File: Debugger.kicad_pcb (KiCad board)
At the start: 2 copper layers, 22 parts, among them J1 Header internal clock, J2 I/O, Q1 BC546, SW1 Single step, U1 NE555P, U2 74LS00, U3 74LS74

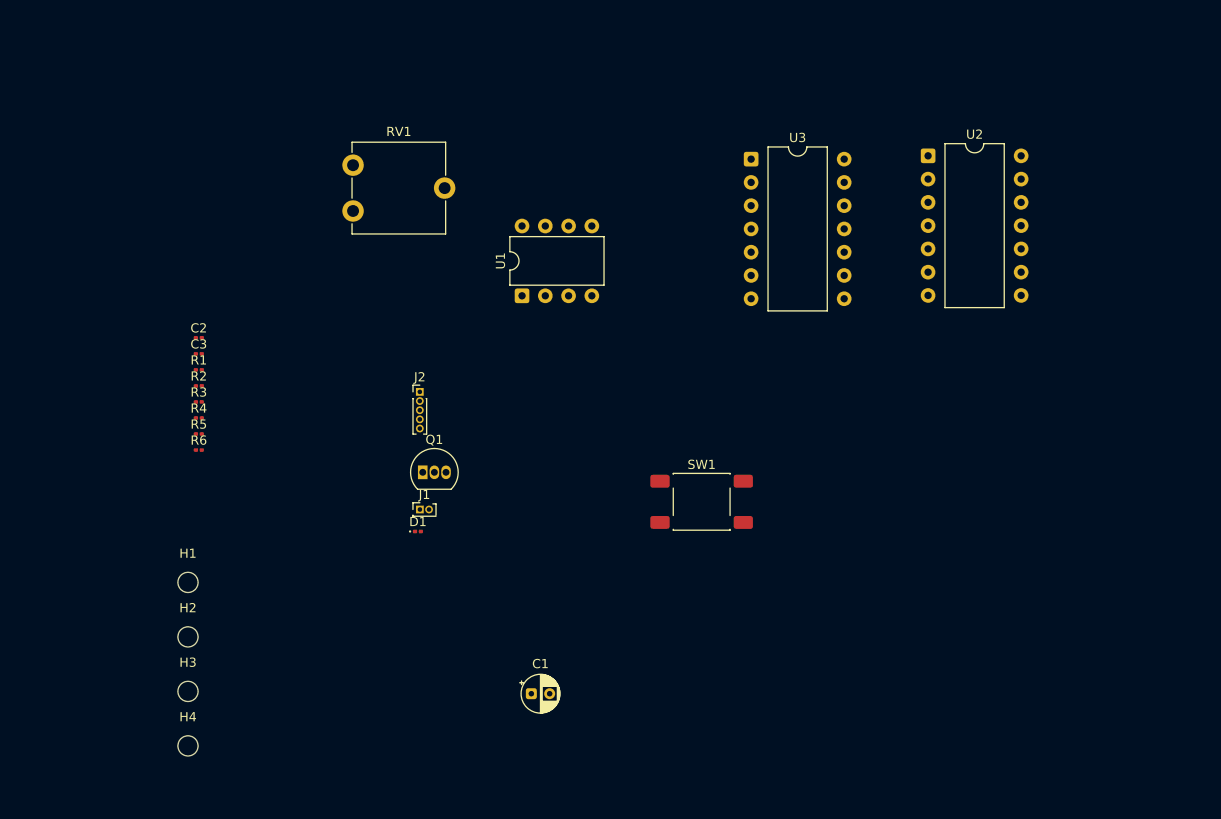
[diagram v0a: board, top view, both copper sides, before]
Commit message: Schematic: schmitt trigger, auxilary ports
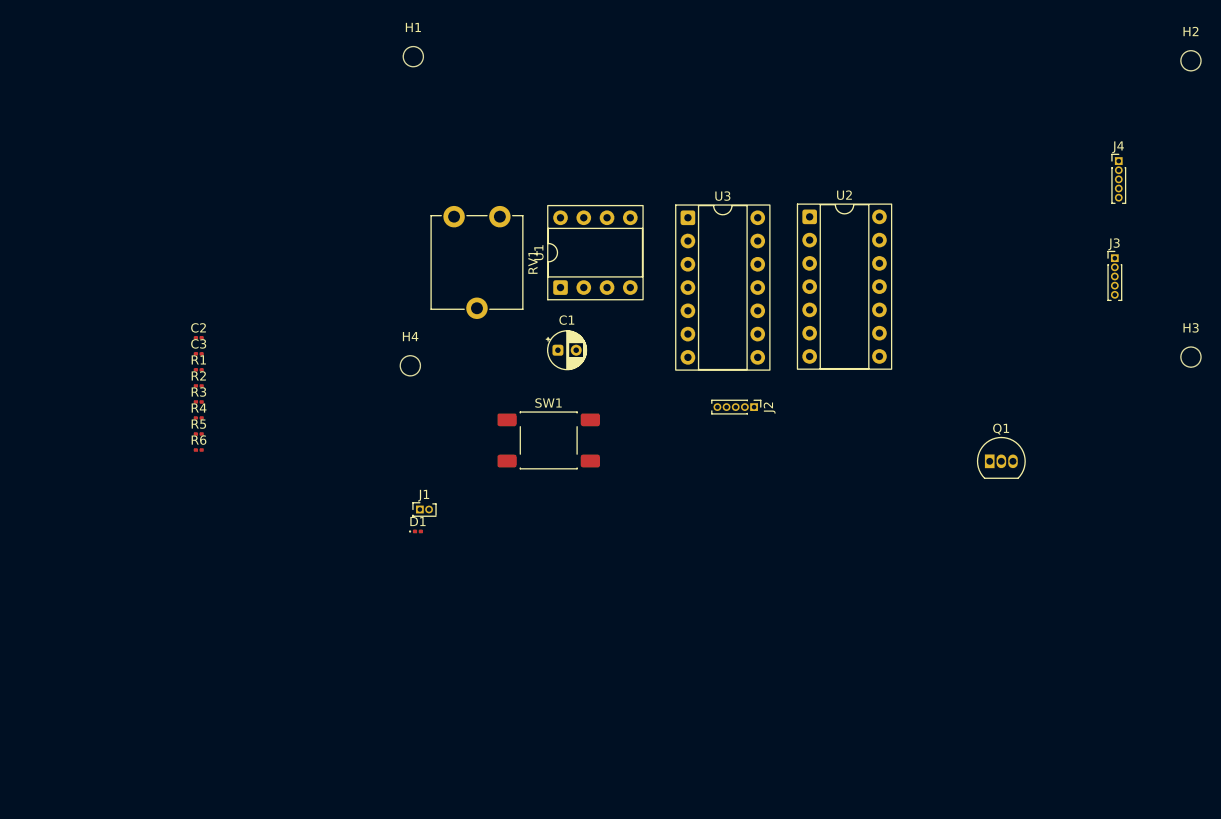
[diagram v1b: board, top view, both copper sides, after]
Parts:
- added J3: NAND0, Connector_PinHeader_1.00mm:PinHeader_1x05_P1.00mm_Vertical, F.Cu at (217.7, 57.2)
- added J4: NAND1, Connector_PinHeader_1.00mm:PinHeader_1x05_P1.00mm_Vertical, F.Cu at (218.1, 46.6)
- J1: value Header internal clock -> Internal clock
- U1: footprint Package_DIP:DIP-8_W7.62mm -> Package_DIP:DIP-8_W7.62mm_Socket
- U2: value 74LS00 -> 74LS132; footprint Package_DIP:DIP-14_W10.16mm -> Package_DIP:DIP-14_W7.62mm_Socket
- U3: footprint Package_DIP:DIP-14_W10.16mm -> Package_DIP:DIP-14_W7.62mm_Socket
- moved H2 126.3 mm to (226.0, 35.7)
- moved H3 115.4 mm to (226.0, 68.0)
- moved H1 62.4 mm to (141.1, 35.2)
- moved Q1 61.9 mm to (204.0, 79.4)
- moved H4 48.1 mm to (140.8, 69.0)
- moved C1 37.6 mm to (156.9, 67.3)
- moved J2 36.5 mm to (178.3, 73.5), turned to -90 degrees
- moved SW1 18.0 mm to (155.9, 77.1)
- moved U2 14.5 mm to (184.3, 52.7)
- moved RV1 11.0 mm to (145.5, 52.7), turned to -90 degrees
- moved U3 9.41 mm to (171.1, 52.8)
- moved U1 4.30 mm to (157.1, 60.4)
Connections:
- J1 pad 1: /OSC -> Net-(J1-Pin_1)
- U1 pad 3: /OSC -> Net-(J1-Pin_1)
- U2 pad 10: (no net) -> Net-(J3-Pin_3)
- U2 pad 11: (no net) -> Net-(J4-Pin_2)
- U2 pad 12: (no net) -> Net-(J4-Pin_4)
- U2 pad 13: (no net) -> Net-(J4-Pin_3)
- U2 pad 4: (no net) -> Net-(J1-Pin_1)
- U2 pad 5: (no net) -> Net-(J1-Pin_1)
- U2 pad 6: (no net) -> /OSC
- U2 pad 8: (no net) -> Net-(J3-Pin_2)
- U2 pad 9: (no net) -> Net-(J3-Pin_4)

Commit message: Board: add PCB drawing
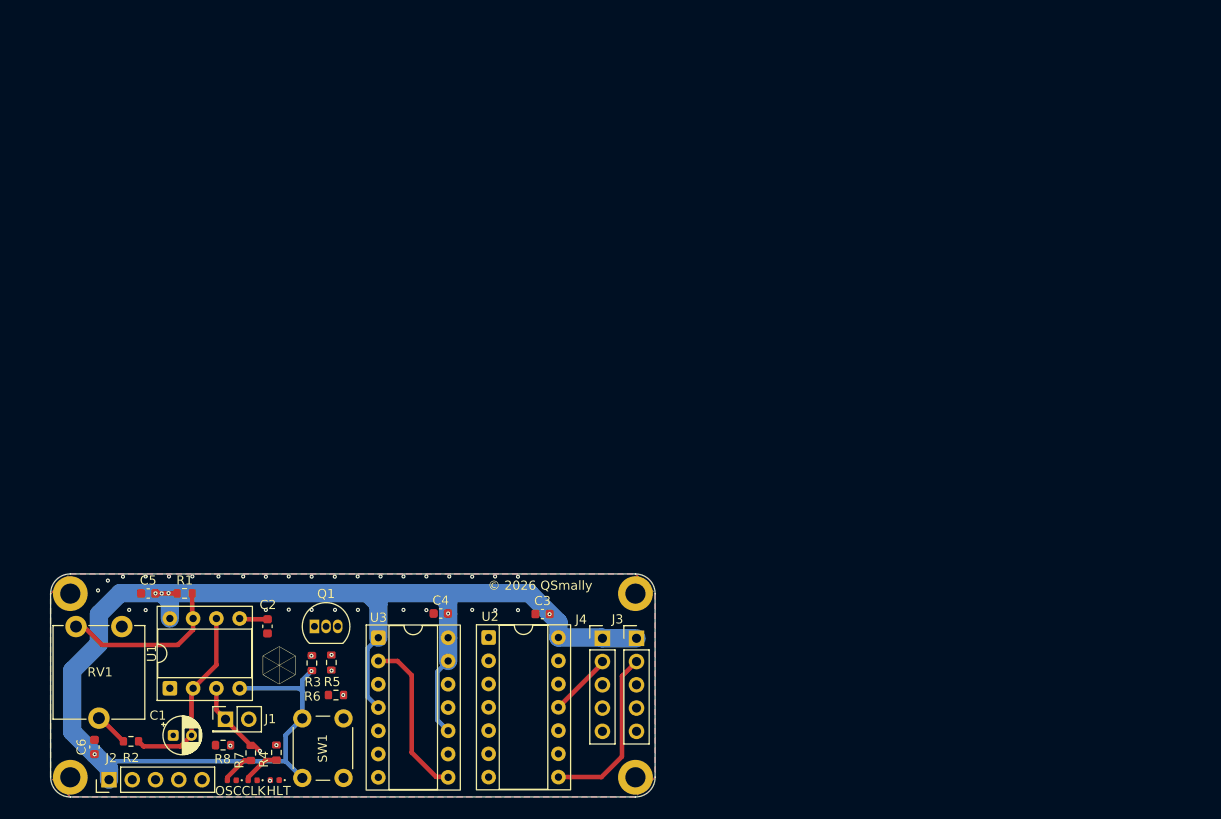
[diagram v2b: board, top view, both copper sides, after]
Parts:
- added C4: 0.1 uF, Capacitor_SMD:C_0603_1608Metric, F.Cu at (144.1, 96.0)
- added C5: 0.1 uF, Capacitor_SMD:C_0603_1608Metric, F.Cu at (112.1, 93.8)
- added C6: 22 uF, Capacitor_SMD:C_0603_1608Metric, F.Cu at (106.3, 110.6)
- added CLK: LED_Small, LED_SMD:LED_0402_1005Metric, F.Cu at (123.5, 114.2)
- added G***: LOGO, LOGO, F.Cu at (126.4, 101.7)
- added OSC: LED_Small, LED_SMD:LED_0402_1005Metric, F.Cu at (121.3, 114.2)
- added R7: 10k, Resistor_SMD:R_0603_1608Metric, F.Cu at (123.3, 111.2)
- added R8: 10k, Resistor_SMD:R_0603_1608Metric, F.Cu at (120.3, 110.4)
- C2, C3: footprint Capacitor_SMD:C_0201_0603Metric -> Capacitor_SMD:C_0603_1608Metric
- H1, H2, H3, H4: footprint MountingHole:MountingHole_2.2mm_M2 -> MountingHole:MountingHole_2.2mm_M2_DIN965_Pad
- HLT: renamed from D1; footprint LED_SMD:LED_0201_0603Metric -> LED_SMD:LED_0402_1005Metric
- J1: footprint Connector_PinHeader_1.00mm:PinHeader_2x01_P1.00mm_Vertical -> Connector_PinHeader_2.54mm:PinHeader_2x01_P2.54mm_Vertical
- J2, J3, J4: footprint Connector_PinHeader_1.00mm:PinHeader_1x05_P1.00mm_Vertical -> Connector_PinHeader_2.54mm:PinHeader_1x05_P2.54mm_Vertical
- R1, R2, R3, R4, R5, R6: footprint Resistor_SMD:R_0201_0603Metric -> Resistor_SMD:R_0603_1608Metric
- SW1: footprint Button_Switch_SMD:SW_Push_1P1T_NO_E-Switch_TL3301NxxxxxG -> Button_Switch_THT:SW_PUSH_6mm
- moved H2 99.0 mm to (165.3, 113.9)
- moved H1 87.1 mm to (103.6, 113.9)
- moved J2 81.3 mm to (107.8, 114.2), turned to 90 degrees
- moved J4 76.8 mm to (161.7, 98.7)
- moved Q1 75.9 mm to (130.3, 97.4)
- moved J3 66.7 mm to (165.4, 98.7)
- moved H3 65.9 mm to (165.3, 93.8)
- moved U1 61.1 mm to (114.5, 104.2)
- moved RV1 60.9 mm to (104.2, 97.4)
- moved C1 59.4 mm to (114.9, 109.3)
- moved U2 57.8 mm to (149.3, 98.6)
- moved U3 57.0 mm to (137.3, 98.7)
- moved C3 47.1 mm to (155.2, 96.1)
- moved SW1 45.6 mm to (129.0, 114.0), turned to 90 degrees
- moved H4 44.7 mm to (103.6, 93.8)
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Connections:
- R4 pad 1: GND -> Net-(D3-A)
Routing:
- net +5V: track 0.00 -> 159.7 mm, vias 0 -> 7
- net /CLK: track 0.00 -> 45.3 mm, vias 0 -> 2
- net Net-(J1-Pin_1): track 0.00 -> 37.6 mm, vias 0 -> 1
- net /OSC: track 0.00 -> 37.5 mm
- net //HALT: track 0.00 -> 25.9 mm, vias 0 -> 1
- net /STEP: track 0.00 -> 22.0 mm, vias 0 -> 1
- net Net-(U1-THRES): track 0.00 -> 20.4 mm
- net Net-(U3A-Q): track 0.00 -> 20.1 mm
- net Net-(D1-A): track 0.00 -> 19.9 mm, vias 0 -> 1
- net Net-(J3-Pin_2): track 0.00 -> 18.9 mm
- net Net-(U3B-Q): track 0.00 -> 18.9 mm
- net Net-(U1-DISCH): track 0.00 -> 18.3 mm
- net Net-(U3A-D): track 0.00 -> 17.8 mm
- net Net-(R3-Pad1): track 0.00 -> 17.8 mm, vias 0 -> 1
- net Net-(J3-Pin_4): track 0.00 -> 12.7 mm
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- added copper zone on B.Cu, net GND
- added copper zone on F.Cu, net GND
- added copper zone on In1.Cu, net GND
- added copper zone on In2.Cu, net GND
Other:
- board outline added: 66 x 24.3 mm
- copper layers 2 -> 4
- board text added: "© 2026 QSmally"

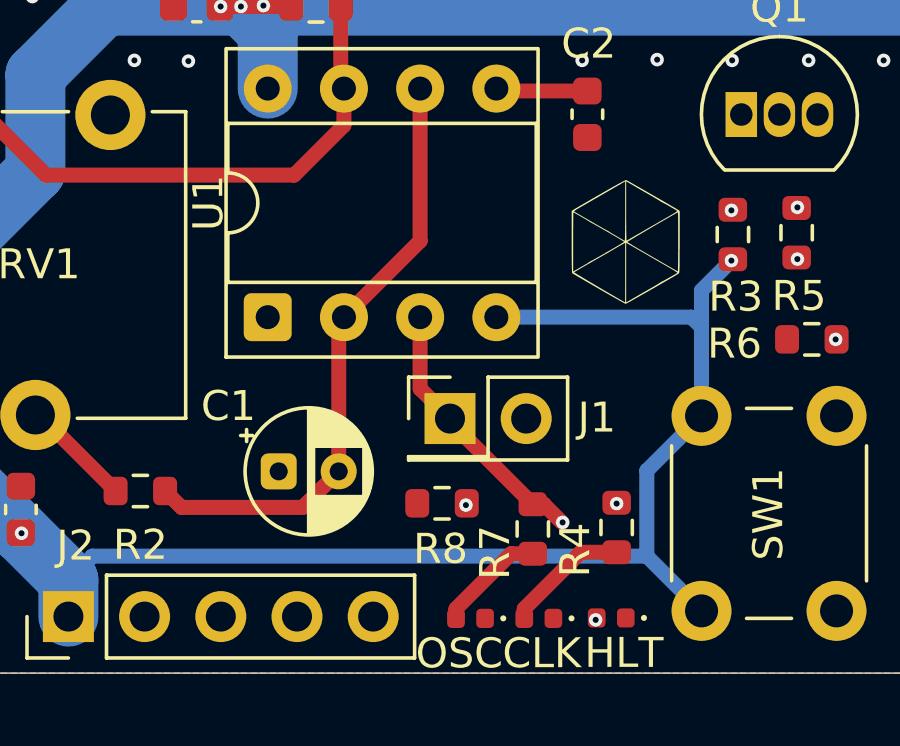
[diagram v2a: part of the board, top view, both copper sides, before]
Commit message: Schematic, Board: fix D1 LED
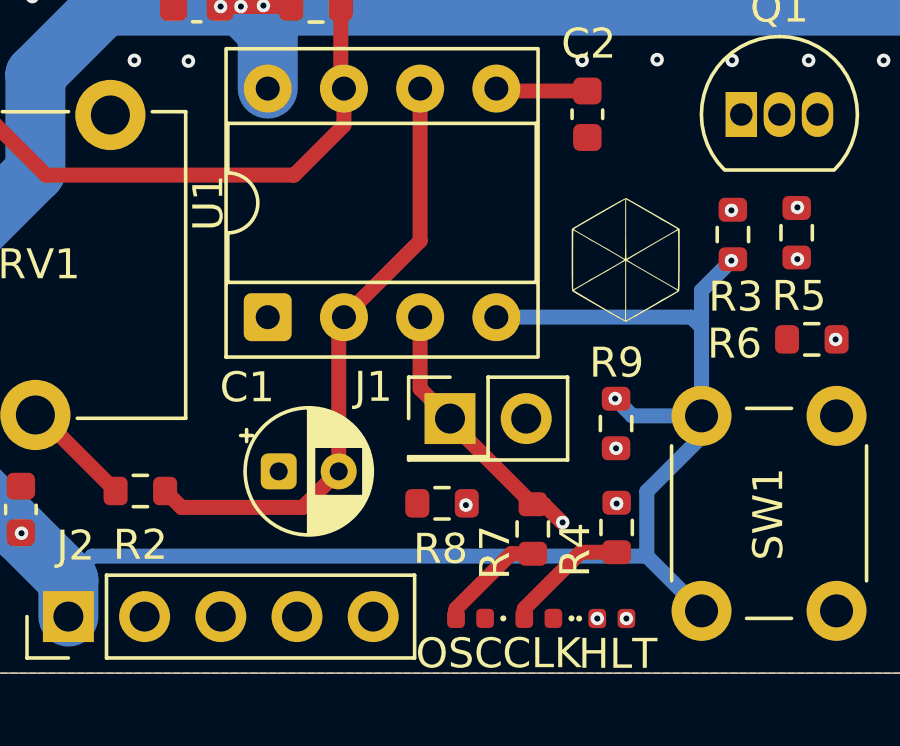
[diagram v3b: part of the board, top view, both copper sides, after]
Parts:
- added R9: 4.7k, Resistor_SMD:R_0603_1608Metric, F.Cu at (126.1, 107.7)
- R4, R7: value 10k -> 4.7k
- moved G*** 0.60 mm to (126.4, 102.3)
- turned HLT to 0 degrees
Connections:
- HLT pad 1: GND -> //HALT
- Q1 pad 3: Net-(D1-A) -> GND
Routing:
- net Net-(D1-A): track 19.9 -> 7.39 mm, vias 1 -> 2
- net //HALT: track 25.9 -> 30.9 mm, vias 1 -> 2
- net +5V: track 159.7 -> 162.8 mm, vias 7 -> 8

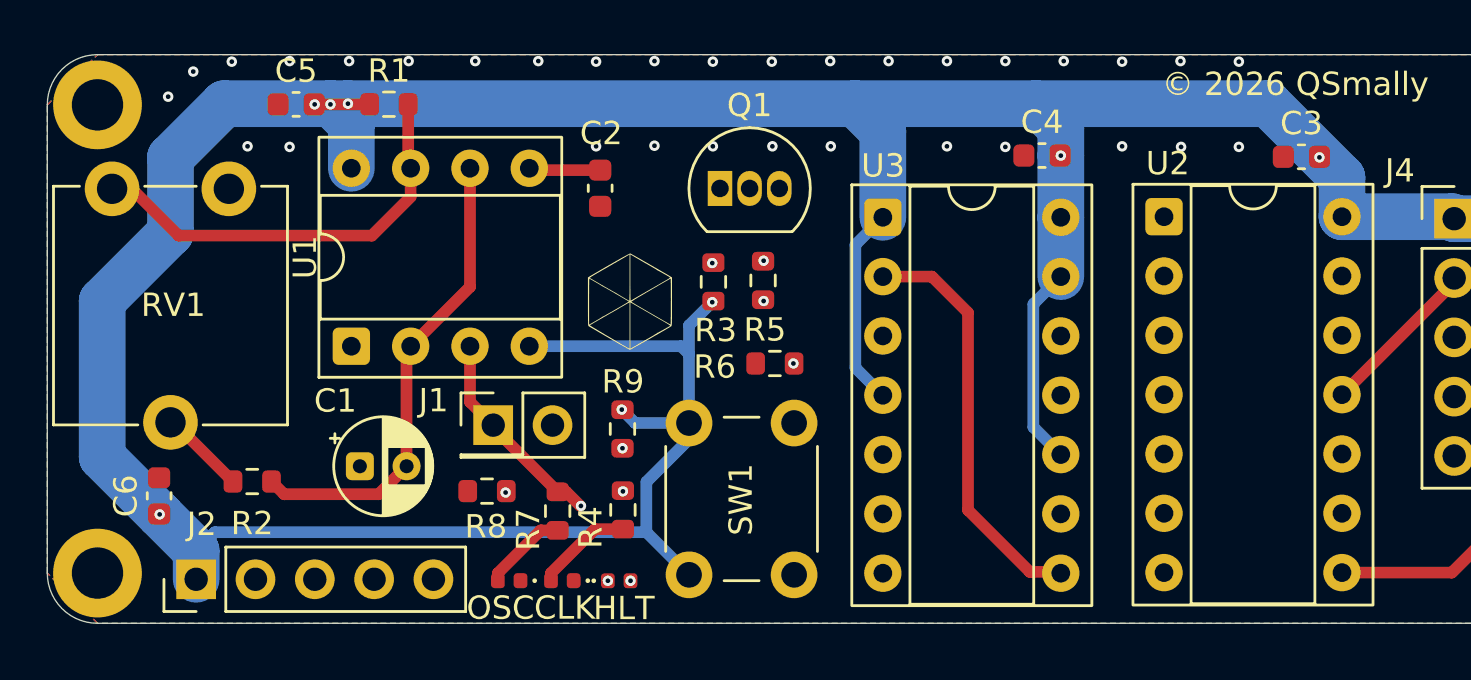
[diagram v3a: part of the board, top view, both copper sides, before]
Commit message: Board: input header consistency
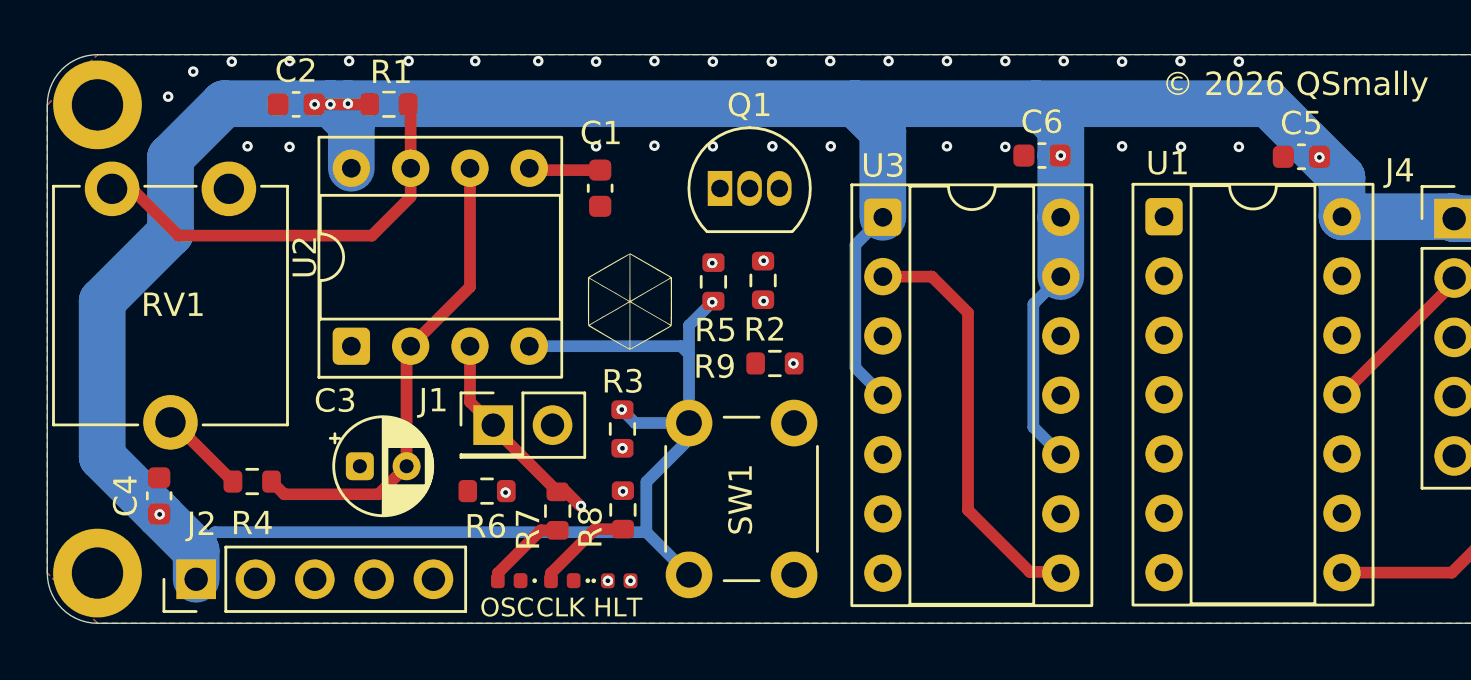
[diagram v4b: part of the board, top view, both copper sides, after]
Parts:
- turned R1 to 180 degrees
- renumbered C2 to C1, C5 to C2, C1 to C3, C6 to C4, C3 to C5, C4 to C6, HLT to D1, OSC to D2, CLK to D3, R5 to R2, R9 to R3, R2 to R4, R3 to R5, R8 to R6, R4 to R8, R6 to R9, U2 to U1, U1 to U2
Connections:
- J2 pad 2: /CLK -> /OSC
- J2 pad 3: /OSC -> /CLK
- R1 pad 1: +5V -> Net-(U2-DISCH)
- R1 pad 2: Net-(U1-DISCH) -> +5V
- RV1 pad 1: Net-(U1-DISCH) -> Net-(U2-DISCH)
- U2 pad 7: Net-(U1-DISCH) -> Net-(U2-DISCH)
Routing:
- net Net-(U1-DISCH): track 18.3 -> 0.00 mm
- net Net-(U2-DISCH): track 0.00 -> 17.8 mm
- net /OSC: track 37.5 -> 42.5 mm
- net /CLK: track 45.3 -> 42.5 mm
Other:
- board text added: "CLK"
- board text added: "HLT"
- board text added: "OSC"

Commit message: Board: revision 2
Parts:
- moved R4 30.8 mm to (113.4, 79.3)
- moved G*** 29.0 mm to (155.3, 99.6)
- moved D1 26.3 mm to (148.0, 99.8)
- moved R3 25.1 mm to (150.1, 100.3)
- moved D3 22.3 mm to (140.6, 99.8), turned to 0 degrees
- moved R6 21.1 mm to (123.2, 89.5), turned to -90 degrees
- moved R8 19.9 mm to (142.8, 100.3)
- moved R9 19.5 mm to (127.2, 86.2), turned to -90 degrees
- moved C1 19.3 mm to (118.4, 79.3), turned to 0 degrees
- moved D2 18.6 mm to (133.1, 99.8), turned to 0 degrees
- moved U1 17.9 mm to (143.5, 81.7)
- moved R1 17.8 mm to (104.8, 80.1), turned to 90 degrees
- moved U3 17.8 mm to (131.7, 81.8)
- moved C6 17.5 mm to (139.3, 79.2)
- moved C5 17.4 mm to (150.8, 79.2)
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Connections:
- J2 pad 2: /OSC -> GND
- J2 pad 3: /CLK -> /OSC
- J2 pad 4: //HALT -> /CLK
- J2 pad 5: GND -> //HALT
- J3 pad 2: Net-(J3-Pin_2) -> GND
- J3 pad 5: GND -> Net-(J3-Pin_5)
- J4 pad 2: Net-(J4-Pin_2) -> GND
- J4 pad 5: GND -> Net-(J4-Pin_5)
- U1 pad 11: Net-(J4-Pin_2) -> Net-(J4-Pin_5)
- U1 pad 8: Net-(J3-Pin_2) -> Net-(J3-Pin_5)
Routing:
- net +5V: track 162.8 -> 193.0 mm, vias 8 -> 5
- net //HALT: track 30.9 -> 58.8 mm
- net Net-(R4-Pad1): track 3.73 -> 25.2 mm
- net Net-(J3-Pin_2): track 18.9 -> 0.00 mm
- net /CLK: track 42.5 -> 54.3 mm, vias 2 -> 0
- net Net-(J3-Pin_5): track 0.00 -> 9.91 mm
- net Net-(J4-Pin_5): track 0.00 -> 9.49 mm
- net Net-(Q1-B): track 3.34 -> 10.6 mm
- net Net-(J4-Pin_2): track 6.99 -> 0.00 mm
- net /OSC: track 42.5 -> 37.0 mm
- net Net-(J1-Pin_1): track 37.6 -> 42.9 mm
- net Net-(D1-A): track 7.39 -> 2.65 mm, vias 2 -> 0
- net /STEP: track 22.0 -> 26.5 mm
- net Net-(U2-DISCH): track 17.8 -> 21.9 mm
- net Net-(J4-Pin_4): track 6.18 -> 9.49 mm
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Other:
- board size 66 x 24.3 mm -> 64 x 24 mm
- board text removed: "© 2026 QSmally"

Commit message: Board, Gerber: fail-safe pot resistor, production
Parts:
- added D4: LED Red, LED_SMD:LED_0603_1608Metric, F.Cu at (119.5, 100.8)
- added R10: 1k, Resistor_SMD:R_0603_1608Metric, F.Cu at (119.5, 99.0)
- added R4: 22k, Resistor_SMD:R_0603_1608Metric, F.Cu at (107.6, 96.8)
- C4: footprint Capacitor_SMD:C_0603_1608Metric -> Capacitor_SMD:C_0805_2012Metric
- D1, D2, D3: value LED_Small -> LED Green; footprint LED_SMD:LED_0402_1005Metric -> LED_SMD:LED_0603_1608Metric
- J1: value Internal clock -> male
- J2: value I/O -> male
- J3: value NAND0 -> male
- J4: value NAND1 -> male
- R3: value 4.7k -> 1k
- R5: renamed from R4; value 220 -> 220R
- R8: renamed from R7; value 4.7k -> 1k
- R9: renamed from R8; value 4.7k -> 1k
- SW1: value Single step -> push button
- moved C4 1.15 mm to (103.9, 97.3), turned to 180 degrees
- moved D1 0.25 mm to (147.7, 99.8)
- moved D2 0.25 mm to (132.9, 99.8)
- moved D3 0.25 mm to (140.4, 99.8)
- moved R3 0.06 mm to (150.1, 100.4)
- renumbered R9 to R11, R5 to R6, R6 to R7
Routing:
- net Net-(U2-DISCH): track 21.9 -> 39.4 mm
- net Net-(U2-THRES): track 18.0 -> 23.5 mm
- net +5V: track 193.0 -> 196.3 mm, vias 5 -> 2
- net Net-(D4-A): track 0.00 -> 2.60 mm
- net //HALT: track 58.8 -> 58.2 mm
- net GND: vias 19 -> 22
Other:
- board text added: "Internal oscillator"
- board text added: "Rev. 2"
- board text added: "Single step"
